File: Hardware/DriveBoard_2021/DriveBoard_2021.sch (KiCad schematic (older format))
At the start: 89 parts, among them SW1 SW_Push, SW2 SW_Push, SW3 SW_Push, SW4 SW_Push, SW5 SW_Push, SW6 SW_Push, SW7 SW_Push, U1 LM2576S-3.3, U2 LM2576HVS-5, U3 TM4C129E_Launchpad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

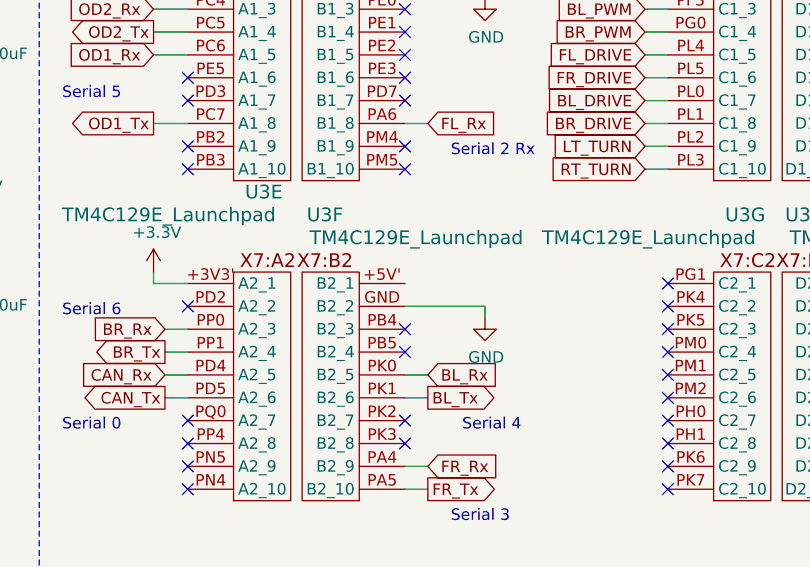
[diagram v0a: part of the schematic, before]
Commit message: All Components and Traces Placed. Silkscreen Updated.
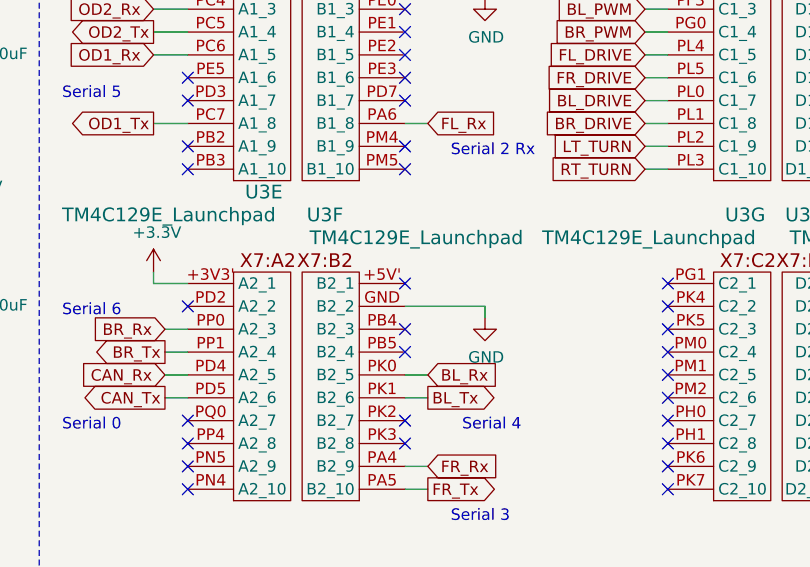
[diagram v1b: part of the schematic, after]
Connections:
- no-connect marks 51 -> 52
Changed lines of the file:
@@
 $EndComp
 $Comp
-L power:GND #PWR?
+L power:GND #PWR0105
 U 1 1 5FB2C97B
 P 1500 3700
-F 0 "#PWR?" H 1500 3450 50  0001 C CNN
+F 0 "#PWR0105" H 1500 3450 50  0001 C CNN
 F 1 "GND" H 1500 3550 50  0000 C CNN
 F 2 "" H 1500 3700 50  0001 C CNN
@@
 Wire Wire Line
 	1500 3700 1500 3650
+NoConn ~ 4850 2400
 $EndSCHEMATC

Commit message: Switched TIVA SMD bottom to THT. Moved Odrive Andersons and re-traced pwr. Added names to LEDs.
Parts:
- U3: footprint MRDT_Shields:TM4C129E_Launchpad_FULL_SMD_BOTTOM -> MRDT_Shields:TM4C129E_Launchpad_FULL_THT_BOTTOM
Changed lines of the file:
@@
 F 0 "U3" H 4150 3200 60  0000 L CNN
 F 1 "TM4C129E_Launchpad" H 3350 3100 60  0000 L CNN
-F 2 "MRDT_Shields:TM4C129E_Launchpad_FULL_SMD_BOTTOM" H 4100 1950 60  0001 C CNN
+F 2 "MRDT_Shields:TM4C129E_Launchpad_FULL_THT_BOTTOM" H 4100 1950 60  0001 C CNN
 F 3 "" H 4100 1950 60  0001 C CNN
 	1    4100 1950
@@
 F 0 "U3" H 4800 3200 60  0000 C CNN
 F 1 "TM4C129E_Launchpad" H 4400 3100 60  0000 C CNN
-F 2 "MRDT_Shields:TM4C129E_Launchpad_FULL_SMD_BOTTOM" H 4650 1950 60  0001 C CNN
+F 2 "MRDT_Shields:TM4C129E_Launchpad_FULL_THT_BOTTOM" H 4650 1950 60  0001 C CNN
 F 3 "" H 4650 1950 60  0001 C CNN
 	2    4650 1950
@@
 F 0 "U3" H 6250 3200 60  0000 L CNN
 F 1 "TM4C129E_Launchpad" H 5450 3100 60  0000 L CNN
-F 2 "MRDT_Shields:TM4C129E_Launchpad_FULL_SMD_BOTTOM" H 6200 1950 60  0001 C CNN
+F 2 "MRDT_Shields:TM4C129E_Launchpad_FULL_THT_BOTTOM" H 6200 1950 60  0001 C CNN
 F 3 "" H 6200 1950 60  0001 C CNN
 	3    6200 1950
@@
 F 0 "U3" H 6900 3200 60  0000 C CNN
 F 1 "TM4C129E_Launchpad" H 6500 3100 60  0000 C CNN
-F 2 "MRDT_Shields:TM4C129E_Launchpad_FULL_SMD_BOTTOM" H 6750 1950 60  0001 C CNN
+F 2 "MRDT_Shields:TM4C129E_Launchpad_FULL_THT_BOTTOM" H 6750 1950 60  0001 C CNN
 F 3 "" H 6750 1950 60  0001 C CNN
 	4    6750 1950
@@
 F 0 "U3" H 4150 4700 60  0000 L CNN
 F 1 "TM4C129E_Launchpad" H 3350 4600 60  0000 L CNN
-F 2 "MRDT_Shields:TM4C129E_Launchpad_FULL_SMD_BOTTOM" H 4100 3350 60  0001 C CNN
+F 2 "MRDT_Shields:TM4C129E_Launchpad_FULL_THT_BOTTOM" H 4100 3350 60  0001 C CNN
 F 3 "" H 4100 3350 60  0001 C CNN
 	5    4100 3350
@@
 F 0 "U3" H 4800 4600 60  0000 C CNN
 F 1 "TM4C129E_Launchpad" H 4400 4500 60  0000 C CNN
-F 2 "MRDT_Shields:TM4C129E_Launchpad_FULL_SMD_BOTTOM" H 4650 3350 60  0001 C CNN
+F 2 "MRDT_Shields:TM4C129E_Launchpad_FULL_THT_BOTTOM" H 4650 3350 60  0001 C CNN
 F 3 "" H 4650 3350 60  0001 C CNN
 	6    4650 3350
@@
 F 0 "U3" H 6250 4600 60  0000 L CNN
 F 1 "TM4C129E_Launchpad" H 5450 4500 60  0000 L CNN
-F 2 "MRDT_Shields:TM4C129E_Launchpad_FULL_SMD_BOTTOM" H 6200 3350 60  0001 C CNN
+F 2 "MRDT_Shields:TM4C129E_Launchpad_FULL_THT_BOTTOM" H 6200 3350 60  0001 C CNN
 F 3 "" H 6200 3350 60  0001 C CNN
 	7    6200 3350
@@
 F 0 "U3" H 6900 4600 60  0000 C CNN
 F 1 "TM4C129E_Launchpad" H 6500 4500 60  0000 C CNN
-F 2 "MRDT_Shields:TM4C129E_Launchpad_FULL_SMD_BOTTOM" H 6750 3350 60  0001 C CNN
+F 2 "MRDT_Shields:TM4C129E_Launchpad_FULL_THT_BOTTOM" H 6750 3350 60  0001 C CNN
 F 3 "" H 6750 3350 60  0001 C CNN
 	8    6750 3350

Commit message: Initial Board Overhaul. Power switched to Okis, re-routing of traces to easier paths. Additional changes.
LEDs given better groupings and silkscreen tags. Given new room with the switch to Okis for regualtors, traces were re-routed to ease the complexity of the board. Odrive trace size changed to 350mil to handle 30A actuation.
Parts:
- removed C1, C2: 100uF, Capacitor_SMD:C_0603_1608Metric_Pad1.05x0.95mm_HandSolder, symbol Device:C_Small
- removed C5, C6: 1000uF, Capacitor_SMD:C_0603_1608Metric_Pad1.05x0.95mm_HandSolder, symbol Device:C_Small
- removed D1, D2: 1N5822, Diode_THT:D_DO-201AD_P15.24mm_Horizontal, symbol Diode:1N5822
- removed F1, F2: Fuse, MRDT_Passives:ATC_Fuse_Block, symbol Device:Fuse_Small
- removed L1, L2: 100uH, Inductor_SMD:L_0603_1608Metric_Pad1.05x0.95mm_HandSolder, symbol Device:L
- removed SW7: SW_Push, Button_Switch_SMD:SW_SPST_TL3305A, symbol Switch:SW_Push
- removed U1: LM2576S-3.3, Package_TO_SOT_SMD:TO-263-5_TabPin3, symbol Regulator_Switching:LM2576S-3.3
- removed U2: LM2576HVS-5, Package_TO_SOT_SMD:TO-263-5_TabPin3, symbol Regulator_Switching:LM2576HVS-5
- added C1, C2, C5, C6: 10uF, Capacitor_SMD:C_0603_1608Metric_Pad1.05x0.95mm_HandSolder, symbol Device:C
- added SW7: SW_SPST, Button_Switch_THT:SW_CuK_JS202011CQN_DPDT_Straight, symbol Switch:SW_SPST
- added U1: OKI 3V3, MRDT_Devices:OKI_Horizontal, symbol MRDT_Devices:OKI
- added U2: OKI 5V, MRDT_Devices:OKI_Horizontal, symbol MRDT_Devices:OKI
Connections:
- wire segments 268 -> 250
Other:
- moved on the sheet: C3, C4, Conn1A, Conn1B, Conn1C

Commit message: Changed Top plane to GND and routed 3V3 traces.
Should fix GND islands.
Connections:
- net +3V3: now also U3.+3V3 (A1_1)
- no-connect marks 52 -> 51
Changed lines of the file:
@@
 NoConn ~ 3900 1500
 NoConn ~ 3900 1100
-NoConn ~ 3900 1000
 NoConn ~ 3900 1600
 NoConn ~ 3900 1800
@@
 	1    0    0    -1
 $EndComp
+$Comp
+L power:+3.3V #PWR?
+U 1 1 5FC8BAC9
+P 3850 950
+F 0 "#PWR?" H 3850 800 50  0001 C CNN
+F 1 "+3.3V" H 3700 1000 50  0000 C CNN
+F 2 "" H 3850 950 50  0001 C CNN
+F 3 "" H 3850 950 50  0001 C CNN
+	1    3850 950
+	1    0    0    -1
+$EndComp
+Wire Wire Line
+	3850 950  3850 1000
+Wire Wire Line
+	3850 1000 3900 1000
 $EndSCHEMATC

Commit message: STEP file fixed, Gerbs Updated, BOM Finished
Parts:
- LED10, LED11, LED12, LED13, LED17, LED18, LED19, LED20, LED21, LED22, LED23, LED24, LED4, LED9: value pink -> yellow
- LED14, LED15, LED16, LED5, LED6, LED7, LED8: value yellow -> blue
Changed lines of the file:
@@
 P 2000 6100
 F 0 "LED5" H 1993 5845 50  0000 C CNN
-F 1 "yellow" H 1993 5936 50  0000 C CNN
+F 1 "blue" H 1993 5936 50  0000 C CNN
 F 2 "LED_SMD:LED_0603_1608Metric_Pad1.05x0.95mm_HandSolder" H 2000 6100 50  0001 C CNN
 F 3 "~" H 2000 6100 50  0001 C CNN
@@
 P 2000 6550
 F 0 "LED6" H 1993 6295 50  0000 C CNN
-F 1 "yellow" H 1993 6386 50  0000 C CNN
+F 1 "blue" H 1993 6386 50  0000 C CNN
 F 2 "LED_SMD:LED_0603_1608Metric_Pad1.05x0.95mm_HandSolder" H 2000 6550 50  0001 C CNN
 F 3 "~" H 2000 6550 50  0001 C CNN
@@
 P 2000 7000
 F 0 "LED7" H 1993 6745 50  0000 C CNN
-F 1 "yellow" H 1993 6836 50  0000 C CNN
+F 1 "blue" H 1993 6836 50  0000 C CNN
 F 2 "LED_SMD:LED_0603_1608Metric_Pad1.05x0.95mm_HandSolder" H 2000 7000 50  0001 C CNN
 F 3 "~" H 2000 7000 50  0001 C CNN
@@
 P 2000 7450
 F 0 "LED8" H 1993 7195 50  0000 C CNN
-F 1 "yellow" H 1993 7286 50  0000 C CNN
+F 1 "blue" H 1993 7286 50  0000 C CNN
 F 2 "LED_SMD:LED_0603_1608Metric_Pad1.05x0.95mm_HandSolder" H 2000 7450 50  0001 C CNN
 F 3 "~" H 2000 7450 50  0001 C CNN
@@
 P 3800 6100
 F 0 "LED14" H 3793 5845 50  0000 C CNN
-F 1 "yellow" H 3793 5936 50  0000 C CNN
+F 1 "blue" H 3793 5936 50  0000 C CNN
 F 2 "LED_SMD:LED_0603_1608Metric_Pad1.05x0.95mm_HandSolder" H 3800 6100 50  0001 C CNN
 F 3 "~" H 3800 6100 50  0001 C CNN
@@
 P 3800 6550
 F 0 "LED15" H 3793 6295 50  0000 C CNN
-F 1 "yellow" H 3793 6386 50  0000 C CNN
+F 1 "blue" H 3793 6386 50  0000 C CNN
 F 2 "LED_SMD:LED_0603_1608Metric_Pad1.05x0.95mm_HandSolder" H 3800 6550 50  0001 C CNN
 F 3 "~" H 3800 6550 50  0001 C CNN
@@
 P 4550 5050
 F 0 "LED18" V 4589 4933 39  0000 R CNN
-F 1 "pink" V 4498 4933 50  0000 R CNN
+F 1 "yellow" V 4498 4933 50  0000 R CNN
 F 2 "LED_SMD:LED_0603_1608Metric_Pad1.05x0.95mm_HandSolder" H 4550 5050 50  0001 C CNN
 F 3 "~" H 4550 5050 50  0001 C CNN
@@
 P 4200 5050
 F 0 "LED17" V 4239 4933 39  0000 R CNN
-F 1 "pink" V 4148 4933 50  0000 R CNN
+F 1 "yellow" V 4148 4933 50  0000 R CNN
 F 2 "LED_SMD:LED_0603_1608Metric_Pad1.05x0.95mm_HandSolder" H 4200 5050 50  0001 C CNN
 F 3 "~" H 4200 5050 50  0001 C CNN
@@
 P 3850 5050
 F 0 "LED13" V 3889 4933 39  0000 R CNN
-F 1 "pink" V 3798 4933 50  0000 R CNN
+F 1 "yellow" V 3798 4933 50  0000 R CNN
 F 2 "LED_SMD:LED_0603_1608Metric_Pad1.05x0.95mm_HandSolder" H 3850 5050 50  0001 C CNN
 F 3 "~" H 3850 5050 50  0001 C CNN
@@
 P 3500 5050
 F 0 "LED12" V 3539 4933 50  0000 R CNN
-F 1 "pink" V 3448 4933 50  0000 R CNN
+F 1 "yellow" V 3448 4933 50  0000 R CNN
 F 2 "LED_SMD:LED_0603_1608Metric_Pad1.05x0.95mm_HandSolder" H 3500 5050 50  0001 C CNN
 F 3 "~" H 3500 5050 50  0001 C CNN
@@
 P 3150 5050
 F 0 "LED11" V 3189 4933 39  0000 R CNN
-F 1 "pink" V 3098 4933 50  0000 R CNN
+F 1 "yellow" V 3098 4933 50  0000 R CNN
 F 2 "LED_SMD:LED_0603_1608Metric_Pad1.05x0.95mm_HandSolder" H 3150 5050 50  0001 C CNN
 F 3 "~" H 3150 5050 50  0001 C CNN
@@
 P 2800 5050
 F 0 "LED10" V 2839 4933 39  0000 R CNN
-F 1 "pink" V 2748 4933 50  0000 R CNN
+F 1 "yellow" V 2748 4933 50  0000 R CNN
 F 2 "LED_SMD:LED_0603_1608Metric_Pad1.05x0.95mm_HandSolder" H 2800 5050 50  0001 C CNN
 F 3 "~" H 2800 5050 50  0001 C CNN
@@
 P 2450 5050
 F 0 "LED9" V 2489 4932 39  0000 R CNN
-F 1 "pink" V 2398 4932 50  0000 R CNN
+F 1 "yellow" V 2398 4932 50  0000 R CNN
 F 2 "LED_SMD:LED_0603_1608Metric_Pad1.05x0.95mm_HandSolder" H 2450 5050 50  0001 C CNN
 F 3 "~" H 2450 5050 50  0001 C CNN
@@
 P 2100 5050
 F 0 "LED4" V 2139 4932 39  0000 R CNN
-F 1 "pink" V 2048 4932 50  0000 R CNN
+F 1 "yellow" V 2048 4932 50  0000 R CNN
 F 2 "LED_SMD:LED_0603_1608Metric_Pad1.05x0.95mm_HandSolder" H 2100 5050 50  0001 C CNN
 F 3 "~" H 2100 5050 50  0001 C CNN
@@
 P 5250 5050
 F 0 "LED20" V 5289 4933 39  0000 R CNN
-F 1 "pink" V 5198 4933 50  0000 R CNN
+F 1 "yellow" V 5198 4933 50  0000 R CNN
 F 2 "LED_SMD:LED_0603_1608Metric_Pad1.05x0.95mm_HandSolder" H 5250 5050 50  0001 C CNN
 F 3 "~" H 5250 5050 50  0001 C CNN
@@
 P 4900 5050
 F 0 "LED19" V 4939 4933 39  0000 R CNN
-F 1 "pink" V 4848 4933 50  0000 R CNN
+F 1 "yellow" V 4848 4933 50  0000 R CNN
 F 2 "LED_SMD:LED_0603_1608Metric_Pad1.05x0.95mm_HandSolder" H 4900 5050 50  0001 C CNN
 F 3 "~" H 4900 5050 50  0001 C CNN
@@
 P 5950 5050
 F 0 "LED22" V 5989 4933 39  0000 R CNN
-F 1 "pink" V 5898 4933 50  0000 R CNN
+F 1 "yellow" V 5898 4933 50  0000 R CNN
 F 2 "LED_SMD:LED_0603_1608Metric_Pad1.05x0.95mm_HandSolder" H 5950 5050 50  0001 C CNN
 F 3 "~" H 5950 5050 50  0001 C CNN
@@
 P 5600 5050
 F 0 "LED21" V 5639 4933 39  0000 R CNN
-F 1 "pink" V 5548 4933 50  0000 R CNN
+F 1 "yellow" V 5548 4933 50  0000 R CNN
 F 2 "LED_SMD:LED_0603_1608Metric_Pad1.05x0.95mm_HandSolder" H 5600 5050 50  0001 C CNN
 F 3 "~" H 5600 5050 50  0001 C CNN
@@
 P 6650 5050
 F 0 "LED24" V 6689 4933 39  0000 R CNN
-F 1 "pink" V 6598 4933 50  0000 R CNN
+F 1 "yellow" V 6598 4933 50  0000 R CNN
 F 2 "LED_SMD:LED_0603_1608Metric_Pad1.05x0.95mm_HandSolder" H 6650 5050 50  0001 C CNN
 F 3 "~" H 6650 5050 50  0001 C CNN
@@
 P 6300 5050
 F 0 "LED23" V 6339 4933 39  0000 R CNN
-F 1 "pink" V 6248 4933 50  0000 R CNN
+F 1 "yellow" V 6248 4933 50  0000 R CNN
 F 2 "LED_SMD:LED_0603_1608Metric_Pad1.05x0.95mm_HandSolder" H 6300 5050 50  0001 C CNN
 F 3 "~" H 6300 5050 50  0001 C CNN
@@
 P 3800 7000
 F 0 "LED16" H 3793 6745 50  0000 C CNN
-F 1 "yellow" H 3793 6836 50  0000 C CNN
+F 1 "blue" H 3793 6836 50  0000 C CNN
 F 2 "LED_SMD:LED_0603_1608Metric_Pad1.05x0.95mm_HandSolder" H 3800 7000 50  0001 C CNN
 F 3 "~" H 3800 7000 50  0001 C CNN
